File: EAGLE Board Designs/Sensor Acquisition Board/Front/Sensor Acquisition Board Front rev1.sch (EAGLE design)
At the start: 39 parts, among them J1 CONNECTOR-SENSOR_NF_S_RA_BLACK, J10 JUMPER_1X02_, J2 CONNECTOR-SENSOR_NF_S_RA_BLACK, J3 CONNECTOR-SENSOR_NF_S_RA_BLACK, J4 CONNECTOR-SENSOR_NF_S_RA_BLACK, J5 CONNECTOR-SENSOR_NF_S_RA_BLACK, J6 CONNECTOR-SENSOR_NF_S_RA_BLACK, J7 CONNECTOR-SENSOR_NF_S_RA_BLACK, J8 CONNECTOR-SENSOR_NF_S_RA_BLACK, J9 CONNECTOR-CAN_NF_S_RA_BLACK, U1 VOLTAGE_REGULATOR_SOT223_5V, U3 TCAN1051HQV-Q1

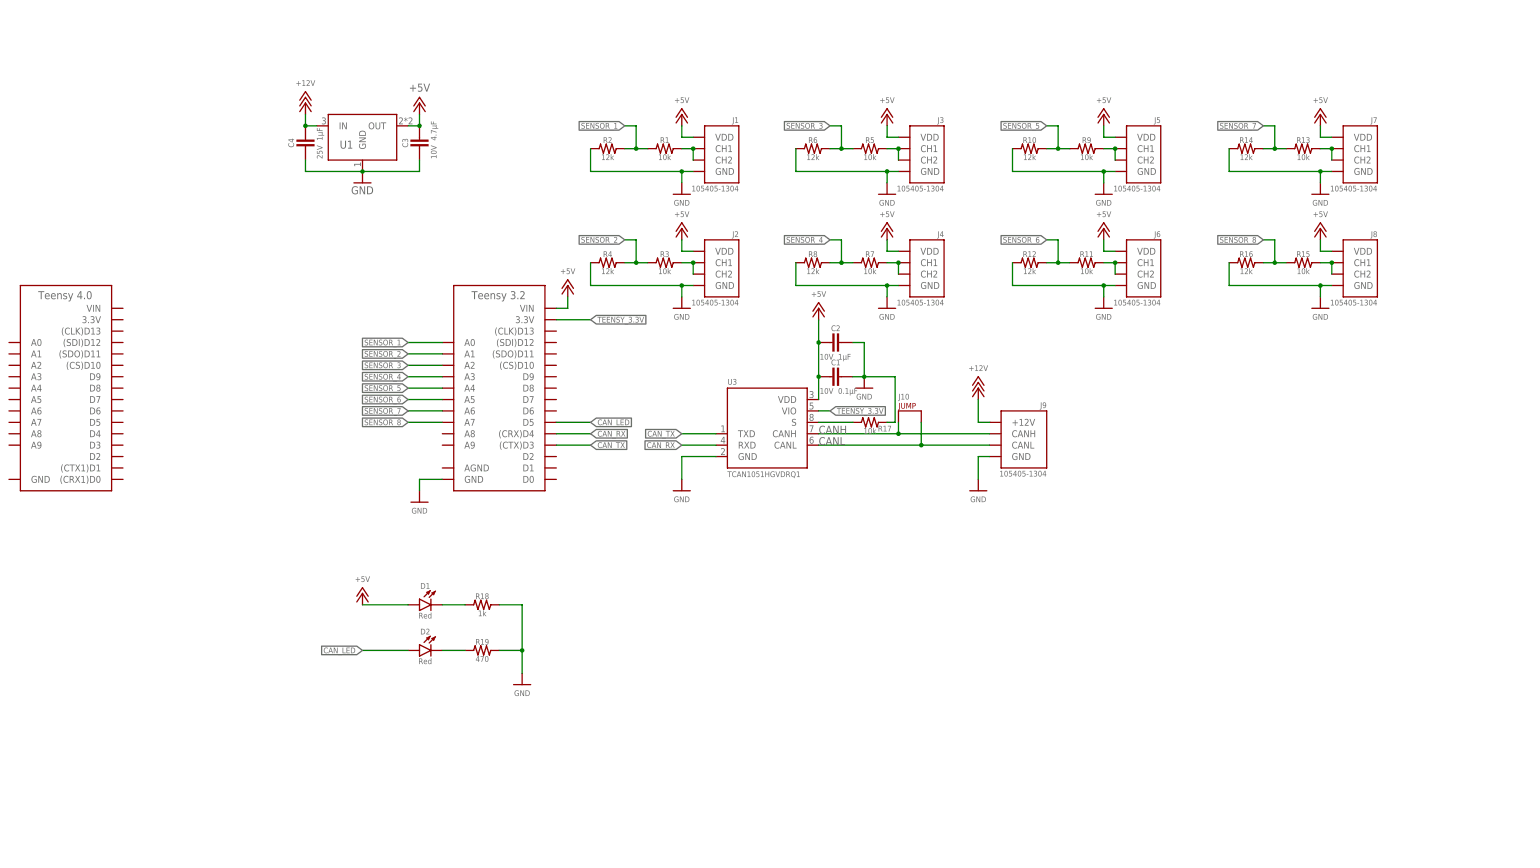
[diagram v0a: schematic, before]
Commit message: Created sch for front rev 1
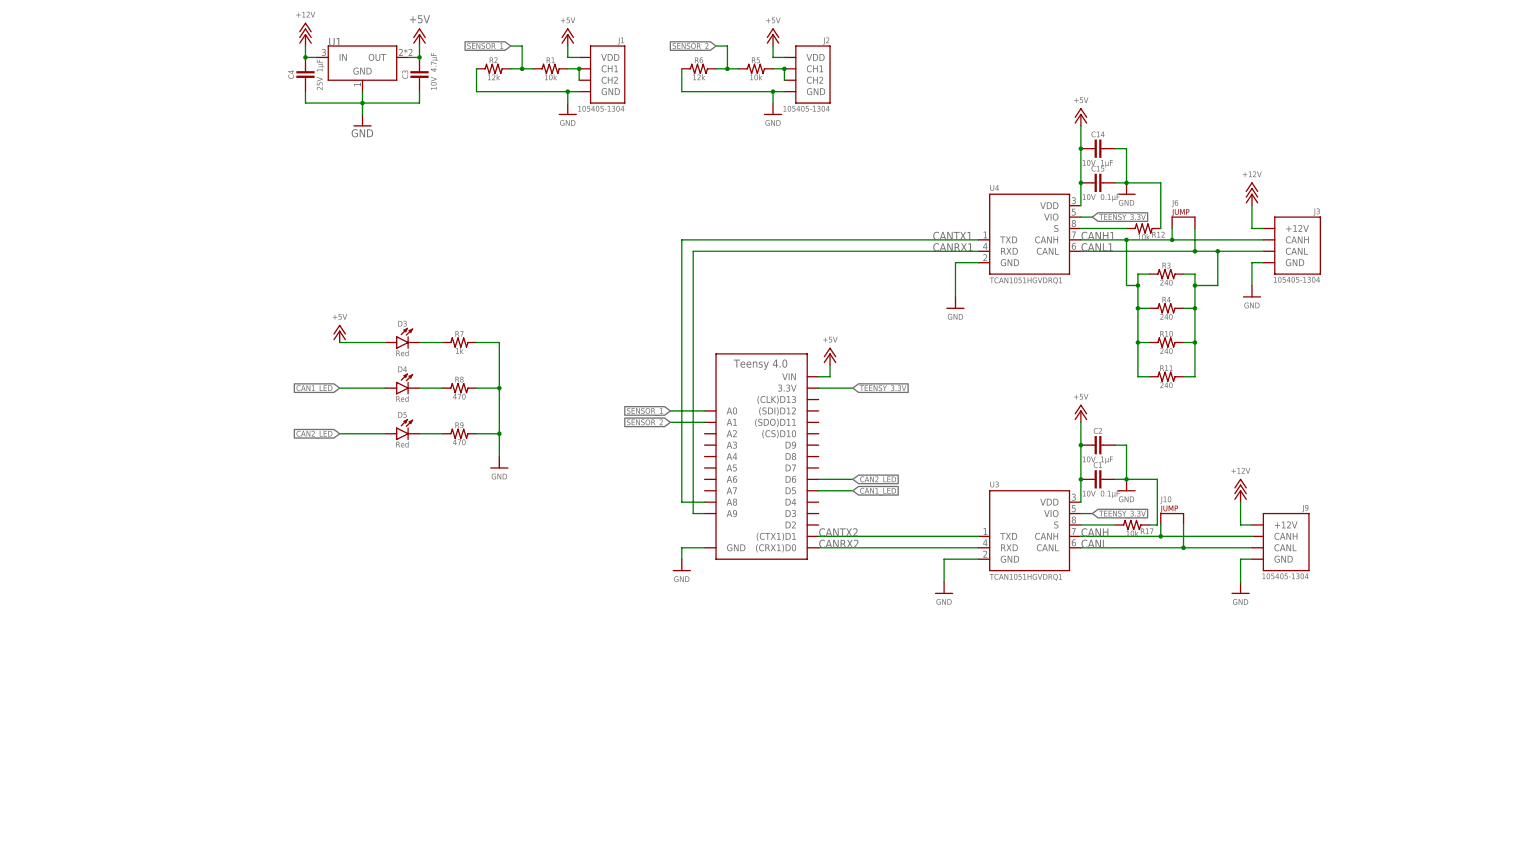
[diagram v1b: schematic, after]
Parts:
- removed A1: TEENSY_3.2, HyTechDevices:TEENSY_3.2
- removed D1, D2: LED_0603_RED, HyTechDevices:LED_0603_RED
- removed J4, J5, J7, J8: CONNECTOR-SENSOR_NF_S_RA_BLACK, HyTechDevices:CONNECTOR-SENSOR_NF_S_RA_BLACK
- removed R13, R15: RESISTOR_0603_10K, HyTechDevices:RESISTOR_0603_10K
- removed R14, R16: RESISTOR_0603_12K, HyTechDevices:RESISTOR_0603_12K
- removed R18: RESISTOR_0603_1K, HyTechDevices:RESISTOR_0603_1K
- removed R19: RESISTOR_0603_470, HyTechDevices:RESISTOR_0603_470
- added C14: CAPACITOR_0603_10V_1UF, HyTechDevices:CAPACITOR_0603_10V_1UF
- added C15: CAPACITOR_0603_10V_0.1UF, HyTechDevices:CAPACITOR_0603_10V_0.1UF
- added D3, D4, D5: LED_0603_RED, HyTechDevices:LED_0603_RED
- added U4: TCAN1051HQV-Q1, HyTechDevices:TCAN1051HQV-Q1
- J10: value JUMPER_1X02_ -> JUMPER_0603_; device HyTechDevices:JUMPER_1X02_ -> HyTechDevices:JUMPER_0603_
- J3: value CONNECTOR-SENSOR_NF_S_RA_BLACK -> CONNECTOR-CAN_NF_S_RA_BLACK; device HyTechDevices:CONNECTOR-SENSOR_NF_S_RA_BLACK -> HyTechDevices:CONNECTOR-CAN_NF_S_RA_BLACK
- J6: value CONNECTOR-SENSOR_NF_S_RA_BLACK -> JUMPER_0603_; device HyTechDevices:CONNECTOR-SENSOR_NF_S_RA_BLACK -> HyTechDevices:JUMPER_0603_
- R10, R4: value RESISTOR_0603_12K -> RESISTOR_0603_240; device HyTechDevices:RESISTOR_0603_12K -> HyTechDevices:RESISTOR_0603_240
- R11, R3: value RESISTOR_0603_10K -> RESISTOR_0603_240; device HyTechDevices:RESISTOR_0603_10K -> HyTechDevices:RESISTOR_0603_240
- R12: value RESISTOR_0603_12K -> RESISTOR_0603_10K; device HyTechDevices:RESISTOR_0603_12K -> HyTechDevices:RESISTOR_0603_10K
- R7: value RESISTOR_0603_10K -> RESISTOR_0603_1K; device HyTechDevices:RESISTOR_0603_10K -> HyTechDevices:RESISTOR_0603_1K
- R8: value RESISTOR_0603_12K -> RESISTOR_0603_470; device HyTechDevices:RESISTOR_0603_12K -> HyTechDevices:RESISTOR_0603_470
- R9: value RESISTOR_0603_10K -> RESISTOR_0603_470; device HyTechDevices:RESISTOR_0603_10K -> HyTechDevices:RESISTOR_0603_470
- U1: value VOLTAGE_REGULATOR_SOT223_5V -> VOLTAGE_REGULATOR_SOT-223_5V; device HyTechDevices:VOLTAGE_REGULATOR_SOT223_5V -> HyTechDevices:VOLTAGE_REGULATOR_SOT-223_5V
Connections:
- removed net CAN_LED: A1.D5, D2.A
- removed net CAN_RX: A1.(CRX)D4, U3.RXD
- removed net CAN_TX: A1.(CTX)D3, U3.TXD
- removed net N$1: D1.C, R18.1
- removed net N$10: J2.CH1, J2.CH2, R3.2
- removed net N$2: D2.C, R19.1
- removed net N$7: J6.CH1, J6.CH2, R11.2
- removed net SENSOR_3: A1.A2, R5.1, R6.2
- removed net SENSOR_4: A1.A3, R7.1, R8.2
- removed net SENSOR_5: A1.A4, R10.2, R9.1
- removed net SENSOR_6: A1.A5, R11.1, R12.2
- removed net SENSOR_7: A1.A6, R13.1, R14.2
- removed net SENSOR_8: A1.A7, R15.1, R16.2
- new net CAN1_LED: A2.D5, D4.A
- new net CAN2_LED: A2.D6, D5.A
- new net CANH1: J3.CANH, J6.1, R10.1, R11.1, R3.1, R4.1, U4.CANH
- new net CANL1: J3.CANL, J6.2, R10.2, R11.2, R3.2, R4.2, U4.CANL
- new net CANRX1: A2.A9, U4.RXD
- new net CANRX2: A2.(CRX1)D0, U3.RXD
- new net CANTX1: A2.A8, U4.TXD
- new net CANTX2: A2.(CTX1)D1, U3.TXD
- net +12V: now also J3.+12V
- net +5V: now also A2.VIN, C14.2, C15.2, D3.A, U4.VDD; no longer A1.VIN, D1.A, J3.VDD, J4.VDD, J5.VDD, J6.VDD, J7.VDD, J8.VDD
- net CANH: now also J10.1; no longer J10.P$1
- net CANL: now also J10.2; no longer J10.P$2
- net GND: now also A2.GND, C14.1, C15.1, R12.2, R7.2, R8.2, R9.2, U4.GND; no longer A1.GND, J4.GND, J5.GND, J6.GND, J7.GND, J8.GND, R10.1, R12.1, R14.1, R16.1, R18.2, R19.2, R4.1, R8.1
- net N$11: now also J2.CH1, J2.CH2; no longer J3.CH1, J3.CH2
- net N$3: now also D3.C, R7.1; no longer J8.CH1, J8.CH2, R15.2
- net N$5: now also D4.C, R8.1; no longer J7.CH1, J7.CH2, R13.2
- net N$6: now also D5.C, R9.1; no longer J5.CH1, J5.CH2, R9.2
- net N$9: now also R12.1, U4.S; no longer J4.CH1, J4.CH2, R7.2
- net SENSOR_1: now also A2.A0; no longer A1.A0
- net SENSOR_2: now also A2.A1, R5.1, R6.2; no longer A1.A1, R3.1, R4.2
- net TEENSY_3.3V: now also A2.3.3V, U4.VIO; no longer A1.3.3V
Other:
- moved on the sheet: C1, C2, C3, C4, J1, J10, J2, J3, J9, R1, R10, R11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

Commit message: Working on front board
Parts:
- removed R17: RESISTOR_0603_10K, HyTechDevices:RESISTOR_0603_10K
- removed U4: TCAN1051HQV-Q1, HyTechDevices:TCAN1051HQV-Q1
- added R13: RESISTOR_0603_10K, HyTechDevices:RESISTOR_0603_10K
- added U2: MCP2562FD, HyTechDevices:MCP2562FD
- U3: value TCAN1051HQV-Q1 -> MCP2562FD; device HyTechDevices:TCAN1051HQV-Q1 -> HyTechDevices:MCP2562FD
- renumbered J9 to J4
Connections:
- removed net N$4: R17.1, U3.S
- removed net N$9: R12.1, U4.S
- new net N$1: R12.2, U2.STBY
- new net N$2: R13.2, U3.STBY
- net +5V: now also U2.VDD; no longer U3.VDD, U4.VDD
- net CANH1: now also U2.CANH; no longer U4.CANH
- net CANL1: now also U2.CANL; no longer U4.CANL
- net CANRX1: now also U2.RXD; no longer U4.RXD
- net CANTX1: now also U2.TXD; no longer U4.TXD
- net GND: now also R12.1, R13.1, U2.GND; no longer R12.2, R17.2, U4.GND
- net TEENSY_3.3V: now also U2.VIO; no longer U4.VIO
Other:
- moved on the sheet: R12, U3

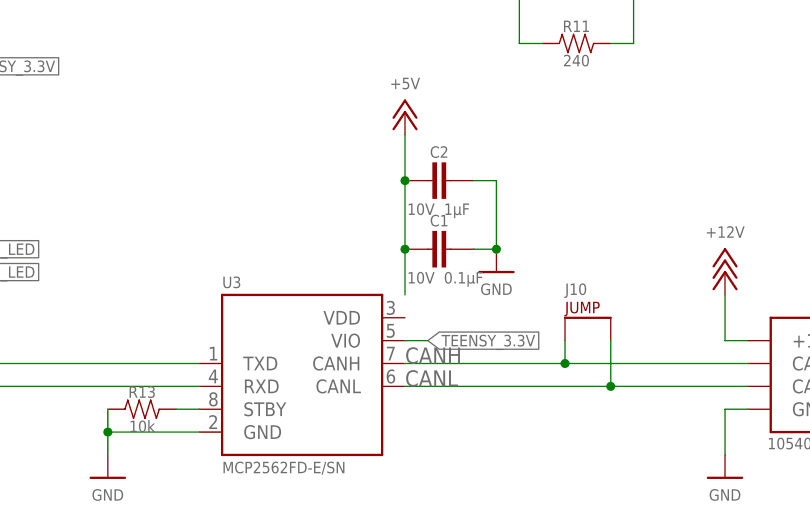
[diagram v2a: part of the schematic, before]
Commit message: Created front board
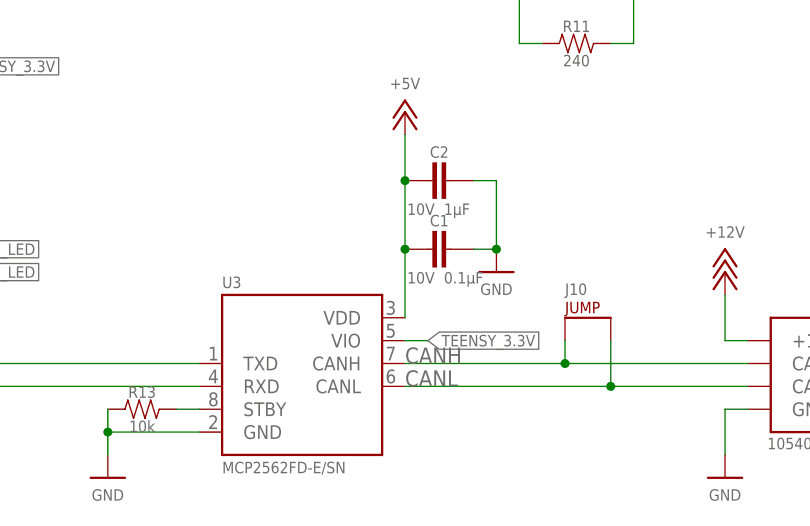
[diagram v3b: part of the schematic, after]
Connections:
- net +5V: now also U3.VDD
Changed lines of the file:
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@@
 <segment>
 <pinref part="C1" gate="G$1" pin="2"/>
-<wire x1="198.12" y1="88.9" x2="198.12" y2="93.98" width="0.1524" layer="91"/>
+<wire x1="198.12" y1="86.36" x2="198.12" y2="93.98" width="0.1524" layer="91"/>
 <wire x1="198.12" y1="93.98" x2="198.12" y2="101.6" width="0.1524" layer="91"/>
 <junction x="198.12" y="93.98"/>
@@
 <wire x1="198.12" y1="101.6" x2="198.12" y2="106.68" width="0.1524" layer="91"/>
 <junction x="198.12" y="101.6"/>
+<pinref part="U3" gate="G$1" pin="VDD"/>
 </segment>
 <segment>
@@
 <segment>
 <pinref part="C15" gate="G$1" pin="2"/>
-<wire x1="198.12" y1="152.4" x2="198.12" y2="160.02" width="0.1524" layer="91"/>
 <wire x1="198.12" y1="160.02" x2="198.12" y2="167.64" width="0.1524" layer="91"/>
-<junction x="198.12" y="160.02"/>
 <pinref part="P+26" gate="1" pin="+5V"/>
 <pinref part="C14" gate="G$1" pin="2"/>
@@
 <junction x="198.12" y="167.64"/>
 <pinref part="U2" gate="G$1" pin="VDD"/>
+<wire x1="198.12" y1="152.4" x2="198.12" y2="160.02" width="0.1524" layer="91"/>
+<junction x="198.12" y="160.02"/>
 </segment>
 <segment>

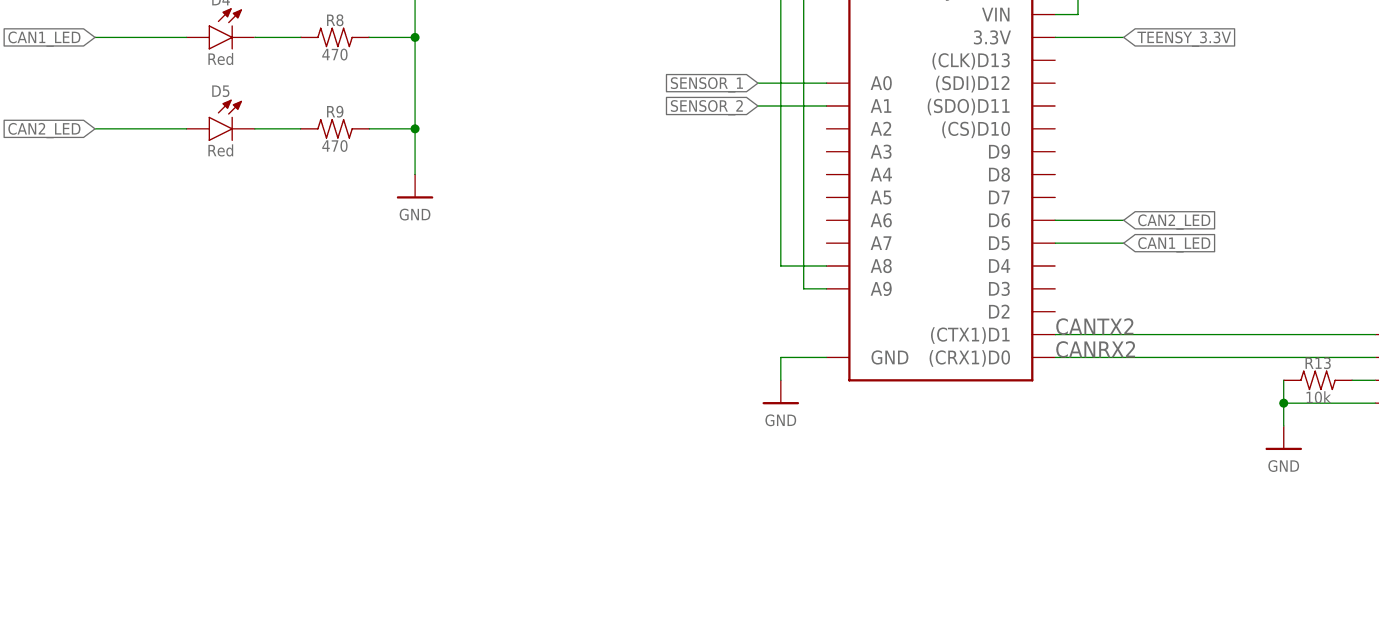
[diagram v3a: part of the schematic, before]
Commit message: connect Ultimate GPS to SAB Front Teensy
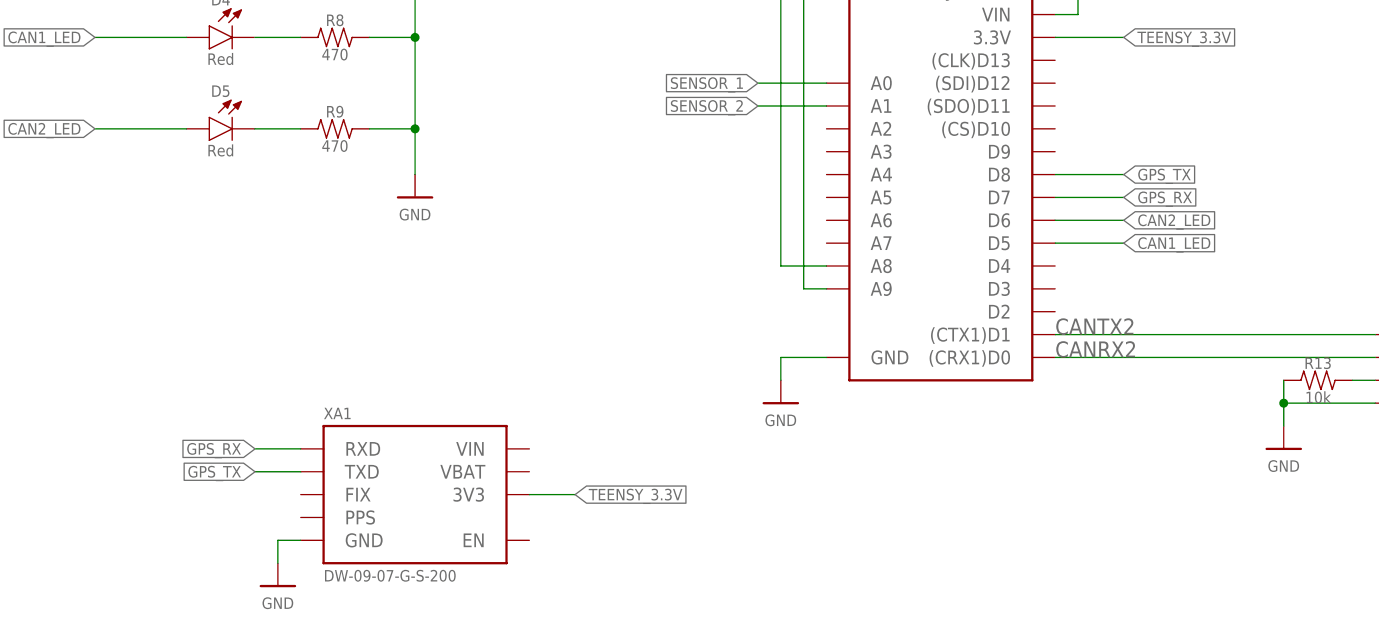
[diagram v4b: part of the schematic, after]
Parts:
- added XA1: ULTIMATE_GPS, HyTechDevices:ULTIMATE_GPS
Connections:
- new net GPS_RX: A2.D7, XA1.RXD
- new net GPS_TX: A2.D8, XA1.TXD
- net GND: now also XA1.GND
- net TEENSY_3.3V: now also XA1.3V3
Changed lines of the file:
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@@
 <setting verticaltext="up"/>
 </settings>
-<grid distance="0.1" unitdist="inch" unit="inch" style="lines" multiple="1" display="yes" altdistance="0.01" altunitdist="inch" altunit="inch"/>
+<grid distance="0.1" unitdist="inch" unit="inch" style="lines" multiple="1" display="no" altdistance="0.01" altunitdist="inch" altunit="inch"/>
 <layers>
 <layer number="1" name="Top" color="4" fill="1" visible="no" active="no"/>
@@
 <part name="R12" library="HyTechDevices" deviceset="RESISTOR_?_*" device="0603" technology="10K"/>
 <part name="R13" library="HyTechDevices" deviceset="RESISTOR_?_*" device="0603" technology="10K"/>
+<part name="XA1" library="HyTechDevices" deviceset="ULTIMATE_GPS" device=""/>
+<part name="P7" library="HyTechSupplies" deviceset="GND" device=""/>
 </parts>
 <sheets>
@@
 <attribute name="RESISTANCE" x="168.91" y="74.93" size="1.27" layer="96" align="top-center"/>
 </instance>
+<instance part="XA1" gate="G$1" x="58.42" y="71.12" smashed="yes">
+<attribute name="NAME" x="58.42" y="71.882" size="1.27" layer="95"/>
+<attribute name="MPN" x="58.42" y="55.118" size="1.27" layer="96" align="top-left"/>
+</instance>
+<instance part="P7" gate="1" x="53.34" y="53.34" smashed="yes">
+<attribute name="VALUE" x="53.34" y="52.07" size="1.27" layer="96" align="top-center"/>
+</instance>
 </instances>
 <busses>
@@
 <junction x="165.1" y="139.7"/>
 </segment>
+<segment>
+<pinref part="XA1" gate="G$1" pin="GND"/>
+<pinref part="P7" gate="1" pin="GND"/>
+<wire x1="55.88" y1="58.42" x2="53.34" y2="58.42" width="0.1524" layer="91"/>
+<wire x1="53.34" y1="58.42" x2="53.34" y2="55.88" width="0.1524" layer="91"/>
+</segment>
 </net>
 <net name="+5V" class="0">
@@
 <pinref part="U2" gate="G$1" pin="VIO"/>
 <wire x1="198.12" y1="149.86" x2="200.66" y2="149.86" width="0.1524" layer="91"/>
+</segment>
+<segment>
+<pinref part="XA1" gate="G$1" pin="3V3"/>
+<wire x1="81.28" y1="63.5" x2="86.36" y2="63.5" width="0.1524" layer="91"/>
+<label x="86.36" y="63.5" size="1.27" layer="95" xref="yes"/>
 </segment>
 </net>
@@
 </segment>
 </net>
+<net name="GPS_RX" class="0">
+<segment>
+<pinref part="XA1" gate="G$1" pin="RXD"/>
+<wire x1="55.88" y1="68.58" x2="50.8" y2="68.58" width="0.1524" layer="91"/>
+<label x="50.8" y="68.58" size="1.27" layer="95" rot="R180" xref="yes"/>
+</segment>
+<segment>
+<pinref part="A2" gate="G$1" pin="D7"/>
+<wire x1="139.7" y1="96.52" x2="147.32" y2="96.52" width="0.1524" layer="91"/>
+<label x="147.32" y="96.52" size="1.27" layer="95" xref="yes"/>
+</segment>
+</net>
+<net name="GPS_TX" class="0">
+<segment>
+<pinref part="XA1" gate="G$1" pin="TXD"/>
+<wire x1="55.88" y1="66.04" x2="50.8" y2="66.04" width="0.1524" layer="91"/>
+<label x="50.8" y="66.04" size="1.27" layer="95" rot="R180" xref="yes"/>
+</segment>
+<segment>
+<pinref part="A2" gate="G$1" pin="D8"/>
+<wire x1="139.7" y1="99.06" x2="147.32" y2="99.06" width="0.1524" layer="91"/>
+<label x="147.32" y="99.06" size="1.27" layer="95" xref="yes"/>
+</segment>
+</net>
